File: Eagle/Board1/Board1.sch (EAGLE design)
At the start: 44 parts, among them IC1 ESP-WROOM-02FRONT-FACE, IC2 NMJ2845-33

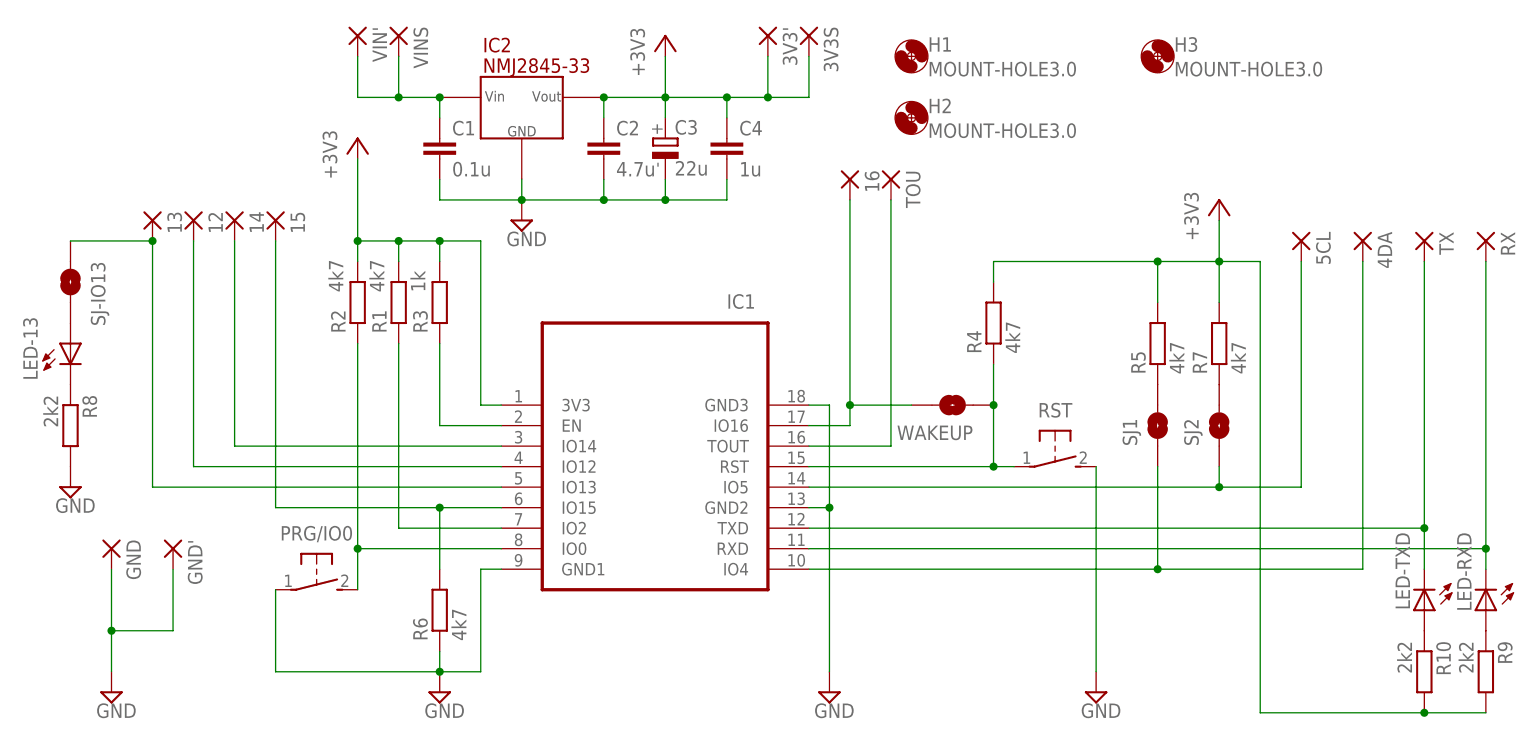
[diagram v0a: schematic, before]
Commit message: ver 1.1 : EN直結, RESET/PROG端子追加 - ENのプルアップ抵抗をやめてVcc直結 - RESET/PROGのPADを追加
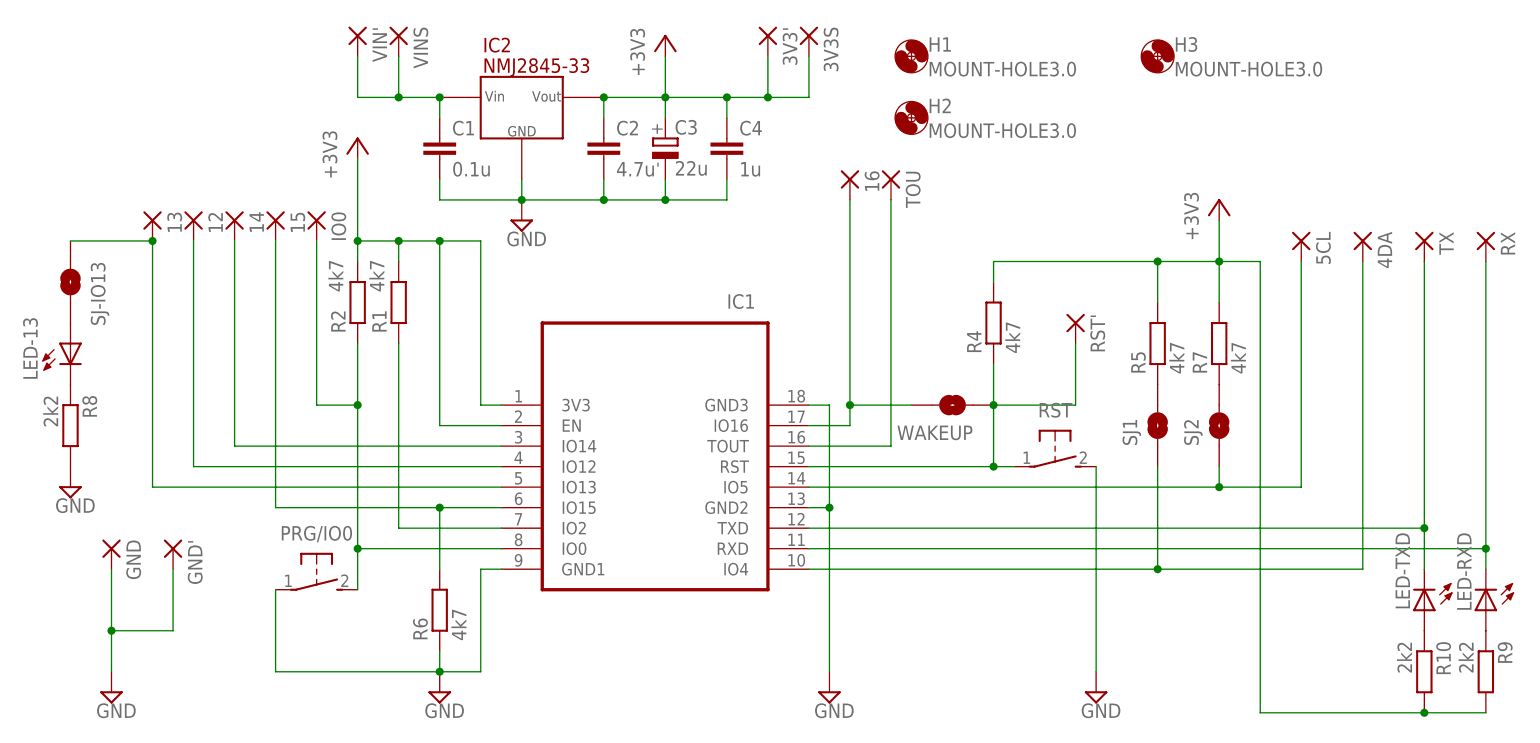
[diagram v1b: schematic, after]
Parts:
- removed R3: 1k, _temp:R-EU_R0603
- added IO0, RST': (no value), wirepad:1,6/0,8
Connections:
- removed net N$1: IC1.EN, R3.1
- net +3V3: now also IC1.EN; no longer R3.2
- net N$2: now also IO0.P
- net N$8: now also RST'.P
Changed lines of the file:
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@@
 <part name="R1" library="_temp" deviceset="R-EU_" device="R0603" value="4k7"/>
 <part name="R2" library="_temp" deviceset="R-EU_" device="R0603" value="4k7"/>
-<part name="R3" library="_temp" deviceset="R-EU_" device="R0603" value="1k"/>
 <part name="R4" library="_temp" deviceset="R-EU_" device="R0603" value="4k7"/>
 <part name="SUPPLY1" library="supply2" deviceset="GND" device=""/>
@@
 <part name="VIN'" library="wirepad" deviceset="1,6/0,8" device=""/>
 <part name="3V3'" library="wirepad" deviceset="1,6/0,8" device=""/>
+<part name="RST'" library="wirepad" deviceset="1,6/0,8" device=""/>
+<part name="IO0" library="wirepad" deviceset="1,6/0,8" device=""/>
 </parts>
 <sheets>
@@
 <attribute name="NAME" x="21.3614" y="77.47" size="1.778" layer="95" rot="R90"/>
 <attribute name="VALUE" x="21.082" y="82.55" size="1.778" layer="96" rot="R90"/>
-</instance>
-<instance part="R3" gate="G$1" x="33.02" y="81.28" smashed="yes" rot="R90">
-<attribute name="NAME" x="31.5214" y="77.47" size="1.778" layer="95" rot="R90"/>
-<attribute name="VALUE" x="31.242" y="82.55" size="1.778" layer="96" rot="R90"/>
 </instance>
 <instance part="R4" gate="G$1" x="101.6" y="78.74" rot="R90"/>
@@
 <instance part="VIN'" gate="P" x="22.86" y="114.3" rot="R270"/>
 <instance part="3V3'" gate="P" x="73.66" y="114.3" rot="R270"/>
+<instance part="RST'" gate="P" x="111.76" y="78.74" rot="R270"/>
+<instance part="IO0" gate="P" x="17.78" y="91.44" rot="R270"/>
 </instances>
 <busses>
@@
 <wire x1="27.94" y1="88.9" x2="27.94" y2="86.36" width="0.1524" layer="91"/>
 <junction x="27.94" y="88.9"/>
-<pinref part="R3" gate="G$1" pin="2"/>
-<wire x1="33.02" y1="88.9" x2="33.02" y2="86.36" width="0.1524" layer="91"/>
+<pinref part="IC1" gate="G$1" pin="EN"/>
+<wire x1="40.64" y1="66.04" x2="33.02" y2="66.04" width="0.1524" layer="91"/>
+<wire x1="33.02" y1="66.04" x2="33.02" y2="88.9" width="0.1524" layer="91"/>
 <junction x="33.02" y="88.9"/>
 </segment>
@@
 </segment>
 </net>
-<net name="N$1" class="0">
-<segment>
-<pinref part="R3" gate="G$1" pin="1"/>
-<wire x1="33.02" y1="76.2" x2="33.02" y2="66.04" width="0.1524" layer="91"/>
-<pinref part="IC1" gate="G$1" pin="EN"/>
-<wire x1="33.02" y1="66.04" x2="40.64" y2="66.04" width="0.1524" layer="91"/>
-</segment>
-</net>
 <net name="N$2" class="0">
 <segment>
@@
 <pinref part="R2" gate="G$1" pin="1"/>
 <wire x1="22.86" y1="50.8" x2="40.64" y2="50.8" width="0.1524" layer="91"/>
-<wire x1="22.86" y1="76.2" x2="22.86" y2="50.8" width="0.1524" layer="91"/>
+<wire x1="22.86" y1="76.2" x2="22.86" y2="68.58" width="0.1524" layer="91"/>
 <junction x="22.86" y="50.8"/>
 <pinref part="PRG/IO0" gate="G$1" pin="2"/>
+<pinref part="IO0" gate="P" pin="P"/>
+<wire x1="22.86" y1="68.58" x2="22.86" y2="50.8" width="0.1524" layer="91"/>
+<wire x1="22.86" y1="68.58" x2="17.78" y2="68.58" width="0.1524" layer="91"/>
+<wire x1="17.78" y1="68.58" x2="17.78" y2="88.9" width="0.1524" layer="91"/>
+<junction x="22.86" y="68.58"/>
 </segment>
 </net>
@@
 <junction x="101.6" y="68.58"/>
 <pinref part="RST" gate="G$1" pin="1"/>
-</segment>
-</net>
+<pinref part="RST'" gate="P" pin="P"/>
+<wire x1="101.6" y1="68.58" x2="111.76" y2="68.58" width="0.1524" layer="91"/>
+<wire x1="111.76" y1="68.58" x2="111.76" y2="76.2" width="0.1524" layer="91"/>
+</segment>
+</net>
